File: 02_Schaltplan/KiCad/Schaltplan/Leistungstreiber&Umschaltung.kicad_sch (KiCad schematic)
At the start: 50 parts, among them J6 MEASURE-CON, J7 MEASURE-CON, J8 MEASURE-CON, J9 MEASURE-CON, Q10 Si2301, Q3 BSS123, Q4 Si2301, Q5 BSS123, Q6 Si2301, Q7 BSS123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

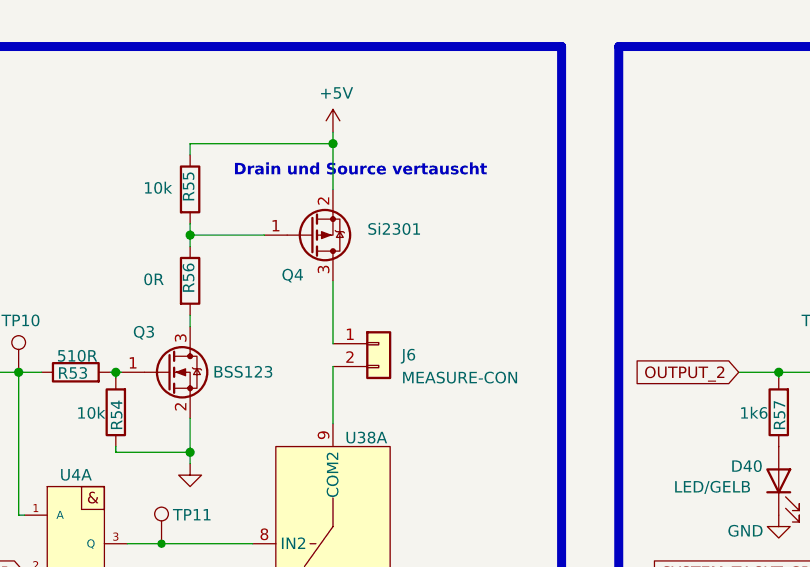
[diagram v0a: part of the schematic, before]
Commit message: ADD
-Dokumentation erweitert
-Schaltplan Fußbeschriftungen
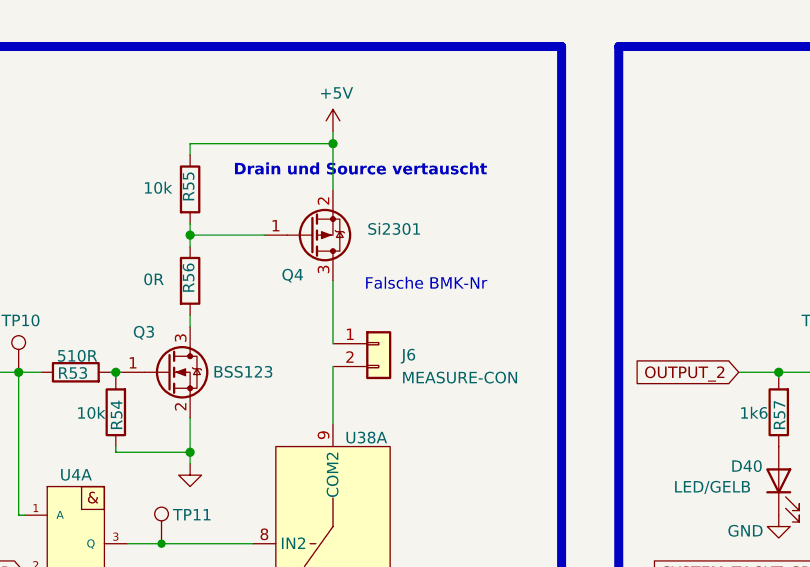
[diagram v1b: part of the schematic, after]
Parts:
- Q4: BMK-Nr 06-6269 -> 08-0150
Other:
- note added: "Falsche BMK-Nr"
- company: (none) -> BMK Group
- title: (none) -> Kabeltester
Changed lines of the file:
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@@
 (kicad_sch (version 20210126) (generator eeschema)
   (paper "User" 540.893 350.012)
+  (title_block
+    (title "Kabeltester")
+    (company "BMK Group")
+    (comment 1 "Erstellt: Maximilian Hoffmann")
+    (comment 2 "Geprüft: Robert Schulz")
+  )
   (junction (at 28.575 309.245) (diameter 1.016) (color 0 0 0 0))
   (junction (at 28.575 329.565) (diameter 1.016) (color 0 0 0 0))
@@
     (effects (font (size 1.27 1.27) (thickness 0.254) bold) (justify right bottom))
   )
+  (text "Falsche BMK-Nr\n" (at 93.345 65.405 180)
+    (effects (font (size 1.27 1.27)) (justify right bottom))
+  )
   (text "Leistungstreiber & Umschaltung\n" (at 325.12 27.305 180)
     (effects (font (size 5 5) (thickness 1) bold) (justify right bottom))
@@
       (effects (font (size 1.27 1.27)) (justify left) hide)
     )
-    (property "BMK-Nr" "06-6269" (id 4) (at 73.66 59.055 0)
-      (effects (font (size 1.27 1.27)) hide)
-    )
+    (property "BMK-Nr" "08-0150" (id 4) (at 73.66 59.055 0)
+      (effects (font (size 1.27 1.27)) hide)
+    )

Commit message: Changes
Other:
- note removed: "DK und KS wurden getauscht"
- note removed: "Drain und Source vertauscht"
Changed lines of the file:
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@@
     (stroke (width 1) (type solid) (color 0 0 255 1))
-  )
-  (text "DK und KS wurden getauscht\n" (at 88.9 117.475 180)
-    (effects (font (size 1.27 1.27)) (justify right bottom))
-  )
-  (text "Drain und Source vertauscht\n" (at 93.345 52.705 180)
-    (effects (font (size 1.27 1.27) (thickness 0.254) bold) (justify right bottom))
   )
   (text "Falsche BMK-Nr\n" (at 93.345 65.405 180)

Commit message: Doku
Schaltplan
-Versorgung
-Taktgeber
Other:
- note removed: "Falsche BMK-Nr"
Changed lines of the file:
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@@
     (stroke (width 1) (type solid) (color 0 0 255 1))
-  )
-  (text "Falsche BMK-Nr\n" (at 93.345 65.405 180)
-    (effects (font (size 1.27 1.27)) (justify right bottom))
   )
   (text "Leistungstreiber & Umschaltung\n" (at 325.12 27.305 180)

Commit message: Änderungen
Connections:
- net SYSTEM_TACKT_SR renamed SYSTEM_TAKT_SR
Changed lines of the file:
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@@
     )
   )
-  (global_label "SYSTEM_TACKT_SR" (shape input) (at 41.91 96.52 180)
+  (global_label "SYSTEM_TAKT_SR" (shape input) (at 41.91 96.52 180)
     (effects (font (size 1.27 1.27)) (justify right))
     (property "Intersheet References" "${INTERSHEET_REFS}" (id 0) (at 20.9186 96.5994 0)
@@
     )
   )
-  (global_label "SYSTEM_TACKT_SR" (shape input) (at 130.81 96.52 180)
+  (global_label "SYSTEM_TAKT_SR" (shape input) (at 130.81 96.52 180)
     (effects (font (size 1.27 1.27)) (justify right))
     (property "Intersheet References" "${INTERSHEET_REFS}" (id 0) (at 109.8186 96.5994 0)
@@
     )
   )
-  (global_label "SYSTEM_TACKT_SR" (shape input) (at 219.71 96.52 180)
+  (global_label "SYSTEM_TAKT_SR" (shape input) (at 219.71 96.52 180)
     (effects (font (size 1.27 1.27)) (justify right))
     (property "Intersheet References" "${INTERSHEET_REFS}" (id 0) (at 198.7186 96.5994 0)
@@
     )
   )
-  (global_label "SYSTEM_TACKT_SR" (shape input) (at 308.61 95.885 180)
+  (global_label "SYSTEM_TAKT_SR" (shape input) (at 308.61 95.885 180)
     (effects (font (size 1.27 1.27)) (justify right))
     (property "Intersheet References" "${INTERSHEET_REFS}" (id 0) (at 287.6186 95.9644 0)

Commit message: ADD
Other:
- note added: "Leitungstreiber & Umschaltung"
- note removed: "Leistungstreiber & Umschaltung"
- moved on the sheet: C44, C45, C46, D39, D40, D41, D42, J6, J7, J8, J9, Q10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

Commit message: ADD
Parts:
- D39, D40, D41, D42: Stromaufnahme (none) -> 1mA
- U38, U39: Stromaufnahme (none) -> 1uA
- U4: Stromaufnahme (none) -> 2uA
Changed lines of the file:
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@@
+      (effects (font (size 1.27 1.27)) hide)
+    )
+    (property "Stromaufnahme" "1mA" (id 4) (at 36.83 73.66 0)
       (effects (font (size 1.27 1.27)) hide)
     )
@@
       (effects (font (size 1.27 1.27)) hide)
     )
+    (property "Stromaufnahme" "1mA" (id 4) (at 36.83 161.925 0)
+      (effects (font (size 1.27 1.27)) hide)
+    )
     (pin "1")
     (pin "2")
@@
       (effects (font (size 1.27 1.27)) hide)
     )
+    (property "Stromaufnahme" "1mA" (id 4) (at 125.73 73.66 0)
+      (effects (font (size 1.27 1.27)) hide)
+    )
     (pin "1")
     (pin "2")
@@
     )
     (property "Mouser" "604-APT1608LSYCKJ3RV" (id 4) (at 214.63 73.66 0)
+      (effects (font (size 1.27 1.27)) hide)
+    )
+    (property "Stromaufnahme" "1mA" (id 4) (at 214.63 73.66 0)
       (effects (font (size 1.27 1.27)) hide)
     )
@@
       (effects (font (size 1.27 1.27)) hide)
     )
+    (property "Stromaufnahme" "2uA" (id 4) (at 193.675 141.605 0)
+      (effects (font (size 1.27 1.27)) hide)
+    )
     (pin "14")
     (pin "7")
@@
       (effects (font (size 1.27 1.27)) hide)
     )
+    (property "Stromaufnahme" "1uA" (id 4) (at 219.075 141.605 0)
+      (effects (font (size 1.27 1.27)) hide)
+    )
     (pin "1")
     (pin "6")
@@
       (effects (font (size 1.27 1.27)) hide)
     )
+    (property "Stromaufnahme" "1uA" (id 4) (at 244.475 141.605 0)
+      (effects (font (size 1.27 1.27)) hide)
+    )
     (pin "1")
     (pin "6")
@@
       (effects (font (size 1.27 1.27)) hide)
     )
+    (property "Stromaufnahme" "2uA" (id 4) (at 47.625 80.645 0)
+      (effects (font (size 1.27 1.27)) hide)
+    )
     (pin "1")
     (pin "2")
@@
     )
     (property "Mouser" "771-HC08PW118" (id 5) (at 55.88 188.595 0)
+      (effects (font (size 1.27 1.27)) hide)
+    )
+    (property "Stromaufnahme" "2uA" (id 4) (at 47.625 168.91 0)
       (effects (font (size 1.27 1.27)) hide)
     )
@@
       (effects (font (size 1.27 1.27)) hide)
     )
+    (property "Stromaufnahme" "2uA" (id 4) (at 136.525 80.645 0)
+      (effects (font (size 1.27 1.27)) hide)
+    )
     (pin "4")
     (pin "5")
@@
       (effects (font (size 1.27 1.27)) hide)
     )
+    (property "Stromaufnahme" "2uA" (id 4) (at 225.425 80.645 0)
+      (effects (font (size 1.27 1.27)) hide)
+    )
     (pin "10")
     (pin "8")
@@
     )
     (property "BMK-Nr" "-" (id 5) (at 51.435 63.5 0)
+      (effects (font (size 1.27 1.27)) hide)
+    )
+    (property "Stromaufnahme" "1uA" (id 4) (at 76.2 80.645 0)
       (effects (font (size 1.27 1.27)) hide)
     )
@@
       (effects (font (size 1.27 1.27)) hide)
     )
+    (property "Stromaufnahme" "1uA" (id 4) (at 76.2 168.91 0)
+      (effects (font (size 1.27 1.27)) hide)
+    )
     (pin "2")
     (pin "3")
@@
     )
     (property "BMK-Nr" "-" (id 5) (at 140.335 97.79 0)
+      (effects (font (size 1.27 1.27)) hide)
+    )
+    (property "Stromaufnahme" "1uA" (id 4) (at 165.1 80.645 0)
       (effects (font (size 1.27 1.27)) hide)
     )
@@
       (effects (font (size 1.27 1.27)) hide)
     )
+    (property "Stromaufnahme" "1uA" (id 4) (at 254 80.645 0)
+      (effects (font (size 1.27 1.27)) hide)
+    )

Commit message: ddd
ADD's
Changes
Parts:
- R52, R57, R62, R67: value 1k6 -> 3k3
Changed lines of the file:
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@@
       (effects (font (size 1.27 1.27)) (justify left))
     )
-    (property "Value" "1k6" (id 1) (at 35.052 66.161 0)
+    (property "Value" "3k3" (id 1) (at 35.052 66.161 0)
       (effects (font (size 1.27 1.27)) (justify left))
     )
@@
       (effects (font (size 1.27 1.27)) (justify left))
     )
-    (property "Value" "1k6" (id 1) (at 35.687 154.426 0)
+    (property "Value" "3k3" (id 1) (at 35.687 154.426 0)
       (effects (font (size 1.27 1.27)) (justify left))
     )
@@
       (effects (font (size 1.27 1.27)) (justify left))
     )
-    (property "Value" "1k6" (id 1) (at 124.587 66.161 0)
+    (property "Value" "3k3" (id 1) (at 124.587 66.161 0)
       (effects (font (size 1.27 1.27)) (justify left))
     )
@@
       (effects (font (size 1.27 1.27)) (justify left))
     )
-    (property "Value" "1k6" (id 1) (at 213.487 66.161 0)
+    (property "Value" "3k3" (id 1) (at 213.487 66.161 0)
       (effects (font (size 1.27 1.27)) (justify left))
     )
@@
       (effects (font (size 1.27 1.27)) hide)
     )
-    (property "Stromaufnahme" "1mA" (id 4) (at 36.83 73.66 0)
+    (property "Stromaufnahme" "1mA" (id 5) (at 36.83 73.66 0)
       (effects (font (size 1.27 1.27)) hide)
     )
@@
       (effects (font (size 1.27 1.27)) hide)
     )
-    (property "Stromaufnahme" "1mA" (id 4) (at 36.83 161.925 0)
+    (property "Stromaufnahme" "1mA" (id 5) (at 36.83 161.925 0)
       (effects (font (size 1.27 1.27)) hide)
     )
@@
       (effects (font (size 1.27 1.27)) hide)
     )
-    (property "Stromaufnahme" "1mA" (id 4) (at 125.73 73.66 0)
+    (property "Stromaufnahme" "1mA" (id 5) (at 125.73 73.66 0)
       (effects (font (size 1.27 1.27)) hide)
     )
@@
       (effects (font (size 1.27 1.27)) hide)
     )
-    (property "Stromaufnahme" "1mA" (id 4) (at 214.63 73.66 0)
-      (effects (font (size 1.27 1.27)) hide)
-    )
+    (property "Stromaufnahme" "1mA" (id 5) (at 214.63 73.66 0)
+      (effects (font (size 1.27 1.27)) hide)
+    )

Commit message: Changes
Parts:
- D39, D40, D41, D42: Mouser 604-APT1608LSYCKJ3RV -> (none)
